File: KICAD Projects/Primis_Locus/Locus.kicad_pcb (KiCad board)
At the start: 2 copper layers, 40 x 40 mm, 50 parts, among them CN1 S2B-PH-SM4-TB_LF_SN, IC1 LSM6DSV16XTR, IC2 QMC6309, J1 Conn_ARM_SWD_TagConnect_TC203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, J4 USB_C_Receptacle_USB2.0_16P, U1 nRF52833_QDxx, U2 TLV70036_SOT23-5, U3 ANT3216LL00R2400A, U4 TP4056-42-ESOP8, Y1 32.768kHz, Y2 32MHz

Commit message: More Locus work
-Just a quick backup of newest work on Locus
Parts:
- removed CN1: S2B-PH-SM4-TB_LF_SN, Connector_JST:JST_PH_S2B-PH-SM4-TB_1x02-1MP_P2.00mm_Horizontal
- removed U4: TP4056-42-ESOP8, Package_SO:SOIC-8-1EP_3.9x4.9mm_P1.27mm_EP2.41x3.3mm_ThermalVias
- added C21: 4.7uF, Capacitor_SMD:C_0805_2012Metric, F.Cu at (181.2, 46.8)
- added D1: LED, LED_SMD:LED_0603_1608Metric, F.Cu at (185.0, 43.2)
- added L3: AN3216-245, primis2:AN3216-245, F.Cu at (214.4, 68.8)
- added R12: 1k, Resistor_SMD:R_0805_2012Metric, F.Cu at (189.2, 49.1)
- added U5: MCP73831T-2ATI_OT, primis2:MCP73831T-2ATI_OT, F.Cu at (185.4, 47.1)
- R11: value 10k -> 8k
- U3: value ANT3216LL00R2400A -> SM02B-GHS-TB_LF_SN; footprint Oscillator:Oscillator_SMD_Silicon_Labs_LGA-6_2.5x3.2mm_P1.25mm -> primis2:SM02B-GHS-TB_LF_SN
- moved U2 86.2 mm to (202.9, 44.5), turned to 180 degrees
- moved C19 77.1 mm to (197.8, 42.0), turned to 90 degrees
- moved C15 76.1 mm to (207.0, 45.6)
- moved D2 62.4 mm to (196.8, 47.5)
- moved R11 59.3 mm to (190.7, 46.0)
- moved C20 50.0 mm to (192.2, 49.0), turned to 90 degrees
- moved J1 43.9 mm to (208.4, 76.6)
- moved R10 41.9 mm to (209.6, 80.5)
- moved C13 41.6 mm to (177.2, 63.5), turned to 90 degrees
- moved C17 39.3 mm to (185.5, 78.8), turned to 90 degrees
- moved R4 38.7 mm to (183.5, 69.3), turned to -90 degrees
- moved C12 37.9 mm to (174.2, 63.5), turned to -90 degrees
- moved U3 37.0 mm to (176.1, 48.3), turned to -90 degrees
- moved R2 33.7 mm to (178.5, 69.3), turned to -90 degrees
- moved R1 32.5 mm to (181.2, 69.3), turned to -90 degrees
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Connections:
- L2 pad 1: Net-(L2-Pad1) -> Net-(L3-RF/Feed/termination)
- U1 pad 7: Net-(U1-P0.11) -> unconnected-(U1-P0.11-Pad7)
- U3 pad 1: Net-(L2-Pad1) -> VDDH
- U3 pad 2: unconnected-(U3-Pad2) -> GND
- U3 pad 3: (no net) -> unconnected-(U3-Pad3)
- U3 pad 4: (no net) -> unconnected-(U3-Pad4)
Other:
- board size 40 x 40 mm -> 50 x 50 mm

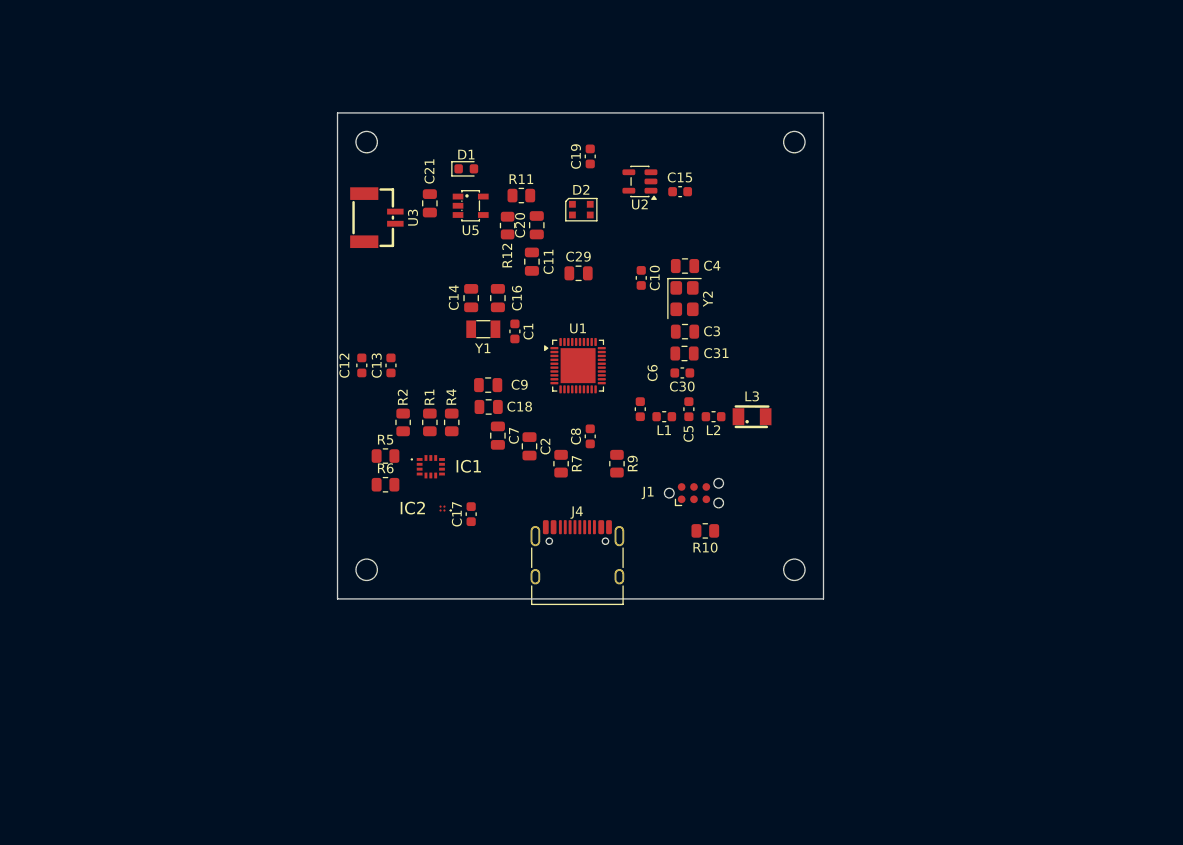
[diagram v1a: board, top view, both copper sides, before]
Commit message: Locus redesign + Some Models
-Locus now uses some 0402 parts
-Removed a bunch of unnecessary parts from Locus
-Shrunk the design down as a result
-Nearly finished routing Locus
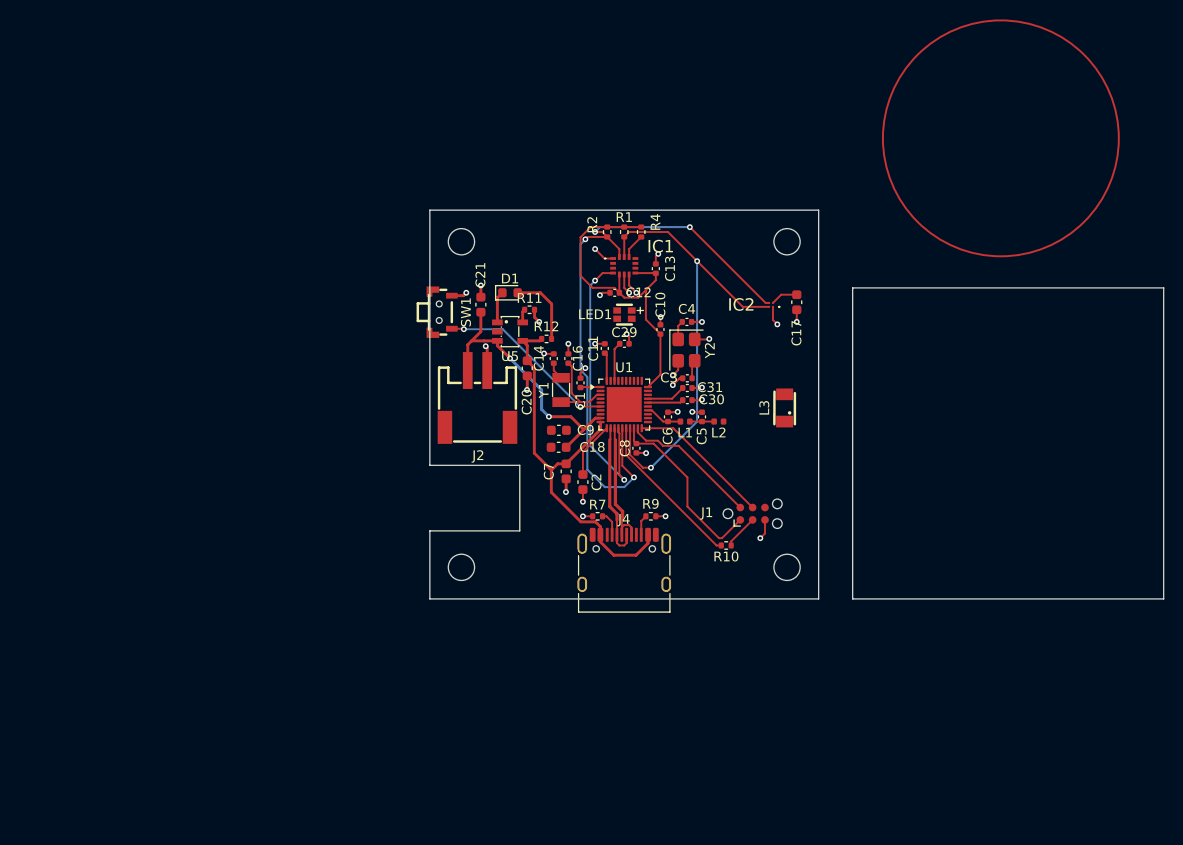
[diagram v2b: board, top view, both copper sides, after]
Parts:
- removed C15, C19: 1uF, Capacitor_SMD:C_0603_1608Metric
- removed D2: WS2812B-2020, LED_SMD:LED_WS2812B-2020_PLCC4_2.0x2.0mm
- removed R5, R6: 10k, Resistor_SMD:R_0805_2012Metric
- removed U2: TLV70036_SOT23-5, Package_TO_SOT_SMD:SOT-23-5
- removed U3: SM02B-GHS-TB_LF_SN, primis2:SM02B-GHS-TB_LF_SN
- added J2: S2B-PH-SM4-TB_LF_SN, primis2:S2B-PH-SM4-TB_LF_SN, F.Cu at (186.2, 66.9)
- added LED1: XL-1615RGBC-RF, primis2:XL-1615RGBC-RF, F.Cu at (201.3, 58.2)
- added SW1: SW_DPST_x2, primis2:SH-1806SA-A3DW-04, F.Cu at (182.5, 58.0)
- C1, C10, C12, C13, C30, C5, C6, C8: footprint Capacitor_SMD:C_0603_1608Metric -> Capacitor_SMD:C_0402_1005Metric
- C11, C14, C16, C29, C3, C31, C4: footprint Capacitor_SMD:C_0805_2012Metric -> Capacitor_SMD:C_0402_1005Metric
- C18, C2, C20, C21, C7, C9: footprint Capacitor_SMD:C_0805_2012Metric -> Capacitor_SMD:C_0603_1608Metric
- H1, H2, H3, H4: footprint MountingHole:MountingHole_2.2mm_M2 -> MountingHole:MountingHole_2.7mm_M2.5
- L1, L2: footprint Inductor_SMD:L_0603_1608Metric -> Inductor_SMD:L_0402_1005Metric
- R1, R10, R11, R12, R2, R4, R7, R9: footprint Resistor_SMD:R_0805_2012Metric -> Resistor_SMD:R_0402_1005Metric
- moved C17 40.0 mm to (219.0, 57.0)
- moved IC2 39.8 mm to (216.3, 57.2)
- moved C13 29.0 mm to (204.5, 53.5)
- moved R2 28.7 mm to (199.5, 49.8)
- moved IC1 28.7 mm to (201.2, 53.2)
- moved R1 28.0 mm to (201.2, 49.8)
- moved R4 27.6 mm to (203.0, 49.8)
- moved C12 27.1 mm to (200.3, 56.0), turned to 0 degrees
- moved C20 14.8 mm to (191.3, 63.8), turned to -90 degrees
- moved H1 14.1 mm to (184.5, 50.8)
- moved U5 13.6 mm to (189.5, 60.0)
- moved D1 13.5 mm to (189.5, 56.0)
- moved R12 12.3 mm to (193.3, 60.8), turned to 180 degrees
- moved R11 11.8 mm to (191.5, 57.8)
- moved C21 11.7 mm to (186.5, 57.2)
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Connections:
- IC1 pad 2: SDX -> GND
- IC1 pad 3: SCX -> GND
- IC2 pad A2: SCX -> SCL
- IC2 pad B2: SDX -> SDA
- U1 pad 33: LED_OUT -> unconnected-(U1-AIN4/P0.28-Pad33)
- U1 pad 34: LED_IN -> unconnected-(U1-AIN5/P0.29-Pad34)
- U1 pad 35: LED_EN -> unconnected-(U1-AIN6/P0.30-Pad35)
- U1 pad 6: unconnected-(U1-P1.09-Pad6) -> Net-(SW1A-A)
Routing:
- net SDA: track 0.00 -> 63.4 mm, vias 0 -> 4
- net VDD_nRF: track 0.00 -> 60.6 mm
- net SCL: track 0.00 -> 49.0 mm, vias 0 -> 2
- net GND: track 0.00 -> 44.0 mm, vias 0 -> 32
- net VBUS: track 0.00 -> 41.3 mm
- net INT: track 0.00 -> 29.9 mm, vias 0 -> 2
- net VDDH: track 0.00 -> 28.1 mm, vias 0 -> 2
- net Net-(SW1A-A): track 0.00 -> 18.7 mm, vias 0 -> 2
- net Net-(U1-P0.18/~{RESET}): track 0.00 -> 16.4 mm
- net Net-(J1-SWCLK): track 0.00 -> 14.8 mm
- net D+: track 0.00 -> 14.2 mm
- net D-: track 0.00 -> 14.2 mm
- net Net-(J1-SWDIO): track 0.00 -> 14.2 mm
- net Net-(U1-XL2/P0.01): track 0.00 -> 8.89 mm
- net DEC4_6: track 0.00 -> 7.72 mm
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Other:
- board size 50 x 50 mm -> 75.5 x 40 mm
- copper layers 2 -> 4

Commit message: Locus EV1 Final
-Finished Locus EV1
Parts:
- added L4: 2450AT18D0100001E, primis2:2450AT18D0100001E, F.Cu at (219.3, 72.5)
- added L5: N.C., Inductor_SMD:L_0402_1005Metric, F.Cu at (217.2, 68.8)
- added R13: 82r, Resistor_SMD:R_0402_1005Metric, F.Cu at (203.2, 61.0)
- added R14: 33r, Resistor_SMD:R_0402_1005Metric, F.Cu at (198.5, 58.8)
- added R15: 33r, Resistor_SMD:R_0402_1005Metric, F.Cu at (198.5, 57.2)
- added R16: 0r, Resistor_SMD:R_0402_1005Metric, F.Cu at (215.5, 69.2)
- added TP1: TestPoint, TestPoint:TestPoint_Pad_1.0x1.0mm, F.Cu at (189.0, 52.5)
- added TP2: TestPoint, TestPoint:TestPoint_Pad_1.0x1.0mm, F.Cu at (194.5, 52.5)
- added TP3: TestPoint, TestPoint:TestPoint_Pad_1.0x1.0mm, F.Cu at (192.5, 83.0)
- added TP4: TestPoint, TestPoint:TestPoint_Pad_1.0x1.0mm, F.Cu at (208.0, 82.8)
- L3: value AN3216-245 -> N.C.; footprint primis2:AN3216-245 -> Inductor_SMD:L_0402_1005Metric
- R11: value 8k -> 5.6k
- moved C3 5.81 mm to (207.5, 59.0), turned to 180 degrees
- moved C4 5.75 mm to (207.8, 64.8), turned to 0 degrees
- moved L3 4.11 mm to (213.8, 68.8)
- turned Y2 to 90 degrees
- renumbered LED1 to D2, IC1 to U2, IC2 to U3
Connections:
- D2 pad 1: unconnected-(LED1-R--Pad1) -> R
- D2 pad 2: unconnected-(LED1-COM+-Pad2) -> VDD_nRF
- D2 pad 3: unconnected-(LED1-B--Pad3) -> B
- D2 pad 4: unconnected-(LED1-G--Pad4) -> G
- L3 pad 2: unconnected-(L3-Solder/termination-Pad2) -> GND
- U1 pad 33: unconnected-(U1-AIN4/P0.28-Pad33) -> Net-(U1-AIN4/P0.28)
- U1 pad 34: unconnected-(U1-AIN5/P0.29-Pad34) -> Net-(U1-AIN5/P0.29)
- U1 pad 35: unconnected-(U1-AIN6/P0.30-Pad35) -> Net-(U1-AIN6/P0.30)
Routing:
- net VDD_nRF: track 60.6 -> 130.7 mm, vias 0 -> 5
- net GND: track 44.0 -> 71.6 mm, vias 32 -> 112
- net DEC4_6: track 7.72 -> 22.4 mm, vias 0 -> 2
- net Net-(U1-AIN6/P0.30): track 0.00 -> 9.64 mm, vias 0 -> 2
- net Net-(U1-AIN5/P0.29): track 0.00 -> 8.36 mm, vias 0 -> 2
- net Net-(U1-XC1): track 1.97 -> 10.2 mm
- net Net-(U1-XL1/P0.00): track 1.81 -> 9.97 mm
- net VBUS: track 41.3 -> 48.3 mm
- net Net-(U1-XC2): track 1.91 -> 8.71 mm
- net VDDH: track 28.1 -> 34.7 mm
- net Net-(L4-FEED/GND): track 0.00 -> 4.18 mm
- net Net-(U1-AIN4/P0.28): track 0.00 -> 3.98 mm
- net Net-(L2-Pad1): track 0.00 -> 3.52 mm
- net R: track 0.00 -> 2.31 mm
- net B: track 0.00 -> 1.74 mm
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- added copper zone on B.Cu, net GND
- added copper zone on F.Cu, net GND
- added copper zone on In1.Cu, net GND
- added copper zone on In2.Cu, net GND
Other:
- board size 75.5 x 40 mm -> 40 x 40 mm

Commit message: Locus EV1 quick fixes
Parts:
- R13: value 82r -> 470r
- R14, R15: value 33r -> 100r
- moved TP3 4.03 mm to (193.0, 79.0)
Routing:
- net VBUS: track 48.3 -> 44.1 mm
- net GND: vias 112 -> 121
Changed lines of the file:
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@@
 	(generator_version "10.0")
 	(general
-		(thickness 1.6)
+		(thickness 1.6062)
 		(legacy_teardrops no)
 	)
@@
 			(layer "dielectric 1"
 				(type "prepreg")
-				(thickness 0.1)
+				(thickness 0.2104)
 				(material "FR4")
 				(epsilon_r 4.5)
@@
 			(layer "In1.Cu"
 				(type "copper")
-				(thickness 0.035)
+				(thickness 0.0152)
 			)
 			(layer "dielectric 2"
 				(type "core")
-				(thickness 1.24)
+				(thickness 1.065)
 				(material "FR4")
 				(epsilon_r 4.5)
@@
 			(layer "In2.Cu"
 				(type "copper")
-				(thickness 0.035)
+				(thickness 0.0152)
 			)
 			(layer "dielectric 3"
 				(type "prepreg")
-				(thickness 0.1)
+				(thickness 0.2104)
 				(material "FR4")
 				(epsilon_r 4.5)
@@
 		(capping no)
 		(filling no)
+		(zone_defaults)
 		(pcbplotparams
 			(layerselection 0x00000000_00000000_55555555_5755f5ff)
@@
 			)
 		)
-		(property "Value" "33r"
+		(property "Value" "100r"
 			(at 0 1.17 0)
 			(layer "F.Fab")
@@
 			)
 		)
-		(property "Value" "33r"
+		(property "Value" "100r"
 			(at 0 1.17 0)
 			(layer "F.Fab")
@@
 	(footprint "TestPoint:TestPoint_Pad_1.0x1.0mm"
 		(layer "F.Cu")
-		(at 192.5 83)
+		(at 193 79)
 		(descr "SMD rectangular pad as test Point, square 1.0mm side length")
 		(tags "test point SMD pad rectangle square")
@@
 			)
 		)
-		(property "Value" "82r"
+		(property "Value" "470r"
 			(at 0 1.17 90)
 			(layer "F.Fab")
@@
 	)
 	(segment
-		(start 192.5 77.777818)
-		(end 193.75 76.527818)
-		(width 0.36)
-		(layer "F.Cu")
-		(net "VBUS")
-	)
-	(segment
 		(start 193.75 74.25)
 		(end 194.4 73.6)
@@
 	)
 	(segment
-		(start 192.5 83)
-		(end 192.5 77.777818)
-		(width 0.36)
-		(layer "F.Cu")
-		(net "VBUS")
-	)
-	(segment
 		(start 192 63.725)
 		(end 191.275 63)
@@
 	)
 	(segment
+		(start 193 77.277818)
+		(end 193 79)
+		(width 0.3)
+		(layer "F.Cu")
+		(net "VBUS")
+	)
+	(segment
 		(start 192.55004 60.94996)
 		(end 192.75 60.75)
@@
 	)
 	(segment
+		(start 193.75 76.527818)
+		(end 193 77.277818)
+		(width 0.3)
+		(layer "F.Cu")
+		(net "VBUS")
+	)
+	(segment
 		(start 198.8 80.071786)
 		(end 198.298214 79.57)
@@
 	)
 	(via
+		(at 202.25 66.5)
+		(size 0.6)
+		(drill 0.3)
+		(layers "F.Cu" "B.Cu")
+		(tenting
+			(front yes)
+			(back yes)
+		)
+		(capping no)
+		(covering
+			(front no)
+			(back no)
+		)
+		(plugging
+			(front no)
+			(back no)
+		)
+		(filling no)
+		(net "GND")
+	)
+	(via
 		(at 219.25 81)
 		(size 0.6)
@@
 	)
 	(via
+		(at 201.25 68.5)
+		(size 0.6)
+		(drill 0.3)
+		(layers "F.Cu" "B.Cu")
+		(tenting
+			(front yes)
+			(back yes)
+		)
+		(capping no)
+		(covering
+			(front no)
+			(back no)
+		)
+		(plugging
+			(front no)
+			(back no)
+		)
+		(filling no)
+		(net "GND")
+	)
+	(via
 		(at 203.5 72.5)
 		(size 0.6)
@@
 	)
 	(via
+		(at 201.25 66.5)
+		(size 0.6)
+		(drill 0.3)
+		(layers "F.Cu" "B.Cu")
+		(tenting
+			(front yes)
+			(back yes)
+		)
+		(capping no)
+		(covering
+			(front no)
+			(back no)
+		)
+		(plugging
+			(front no)
+			(back no)
+		)
+		(filling no)
+		(net "GND")
+	)
+	(via
 		(at 211.5 74.75)
 		(size 0.6)
@@
 	)
 	(via
+		(at 200.25 66.5)
+		(size 0.6)
+		(drill 0.3)
+		(layers "F.Cu" "B.Cu")
+		(tenting
+			(front yes)
+			(back yes)
+		)
+		(capping no)
+		(covering
+			(front no)
+			(back no)
+		)
+		(plugging
+			(front no)
+			(back no)
+		)
+		(filling no)
+		(net "GND")
+	)
+	(via
 		(at 216.75 54)
 		(size 0.6)
@@
 	)
 	(via
+		(at 201.25 67.5)
+		(size 0.6)
+		(drill 0.3)
+		(layers "F.Cu" "B.Cu")
+		(tenting
+			(front yes)
+			(back yes)
+		)
+		(capping no)
+		(covering
+			(front no)
+			(back no)
+		)
+		(plugging
+			(front no)
+			(back no)
+		)
+		(filling no)
+		(net "GND")
+	)
+	(via
+		(at 200.25 67.5)
+		(size 0.6)
+		(drill 0.3)
+		(layers "F.Cu" "B.Cu")
+		(tenting
+			(front yes)
+			(back yes)
+		)
+		(capping no)
+		(covering
+			(front no)
+			(back no)
+		)
+		(plugging
+			(front no)
+			(back no)
+		)
+		(filling no)
+		(net "GND")
+	)
+	(via
 		(at 215.5 53)
 		(size 0.6)
@@
 	)
 	(via
+		(at 202.25 68.5)
+		(size 0.6)
+		(drill 0.3)
+		(layers "F.Cu" "B.Cu")
+		(tenting
+			(front yes)
+			(back yes)
+		)
+		(capping no)
+		(covering
+			(front no)
+			(back no)
+		)
+		(plugging
+			(front no)
+			(back no)
+		)
+		(filling no)
+		(net "GND")
+	)
+	(via
 		(at 214.208333 48.5)
 		(size 0.6)
@@
 	)
 	(via
+		(at 200.25 68.5)
+		(size 0.6)
+		(drill 0.3)
+		(layers "F.Cu" "B.Cu")
+		(tenting
+			(front yes)
+			(back yes)
+		)
+		(capping no)
+		(covering
+			(front no)
+			(back no)
+		)
+		(plugging
+			(front no)
+			(back no)
+		)
+		(filling no)
+		(net "GND")
+	)
+	(via
 		(at 191.25 66)
 		(size 0.6)
@@
 	)
 	(via
+		(at 202.25 67.5)
+		(size 0.6)
+		(drill 0.3)
+		(layers "F.Cu" "B.Cu")
+		(tenting
+			(front yes)
+			(back yes)
+		)
+		(capping no)
+		(covering
+			(front no)
+			(back no)
+		)
+		(plugging
+			(front no)
+			(back no)
+		)
+		(filling no)
+		(net "GND")
+	)
+	(via
 		(at 208 58)
 		(size 0.6)
@@
 	)
 	(segment
+		(start 217.25 69.25)
+		(end 218.25 69.25)
+		(width 0.36)
+		(layer "F.Cu")
+		(net "Net-(L4-FEED{slash}GND)")
+	)
+	(segment
+		(start 218.7 69.7)
+		(end 218.25 69.25)
+		(width 0.36)
+		(layer "F.Cu")
+		(net "Net-(L4-FEED{slash}GND)")
+	)
+	(segment
+		(start 216.01 69.25)
+		(end 217.25 69.25)
+		(width 0.36)
+		(layer "F.Cu")
+		(net "Net-(L4-FEED{slash}GND)")
+	)
+	(segment
+		(start 218.7 71)
+		(end 218.7 69.7)
+		(width 0.36)
+		(layer "F.Cu")
+		(net "Net-(L4-FEED{slash}GND)")
+	)
+	(segment
+		(start 213.75 69.25)
+		(end 214.99 69.25)
+		(width 0.36)
+		(layer "F.Cu")
+		(net "Net-(L2-Pad1)")
+	)
+	(segment
+		(start 211.47 69.25)
+		(end 213.75 69.25)
+		(width 0.36)
+		(layer "F.Cu")
+		(net "Net-(L2-Pad1)")
+	)
+	(segment
 		(start 212.25 81.579)
 		(end 212.25 82)
@@
 	)
 	(segment
-		(start 217.25 69.25)
-		(end 218.25 69.25)
-		(width 0.36)
-		(layer "F.Cu")
-		(net "Net-(L4-FEED{slash}GND)")
-	)
-	(segment
-		(start 218.7 69.7)
-		(end 218.25 69.25)
-		(width 0.36)
-		(layer "F.Cu")
-		(net "Net-(L4-FEED{slash}GND)")
-	)
-	(segment
-		(start 216.01 69.25)
-		(end 217.25 69.25)
-		(width 0.36)
-		(layer "F.Cu")
-		(net "Net-(L4-FEED{slash}GND)")
-	)
-	(segment
-		(start 218.7 71)
-		(end 218.7 69.7)
-		(width 0.36)
-		(layer "F.Cu")
-		(net "Net-(L4-FEED{slash}GND)")
-	)
-	(segment
 		(start 203 79.48)
 		(end 203.48 79)
@@
 		(net "Net-(D1-K)")
 	)
-	(segment
-		(start 213.75 69.25)
-		(end 214.99 69.25)
-		(width 0.36)
-		(layer "F.Cu")
-		(net "Net-(L2-Pad1)")
-	)
-	(segment
-		(start 211.47 69.25)
-		(end 213.75 69.25)
-		(width 0.36)
-		(layer "F.Cu")
-		(net "Net-(L2-Pad1)")
-	)
 	(zone
